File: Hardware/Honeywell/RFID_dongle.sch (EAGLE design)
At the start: 11 parts, among them J1 USB_B_PTH, J2 USB_A_PTH_MALE, J5 1X2-3.5MM, J6 1X2-3.5MM, Q1 35A/25V/8.5mΩ

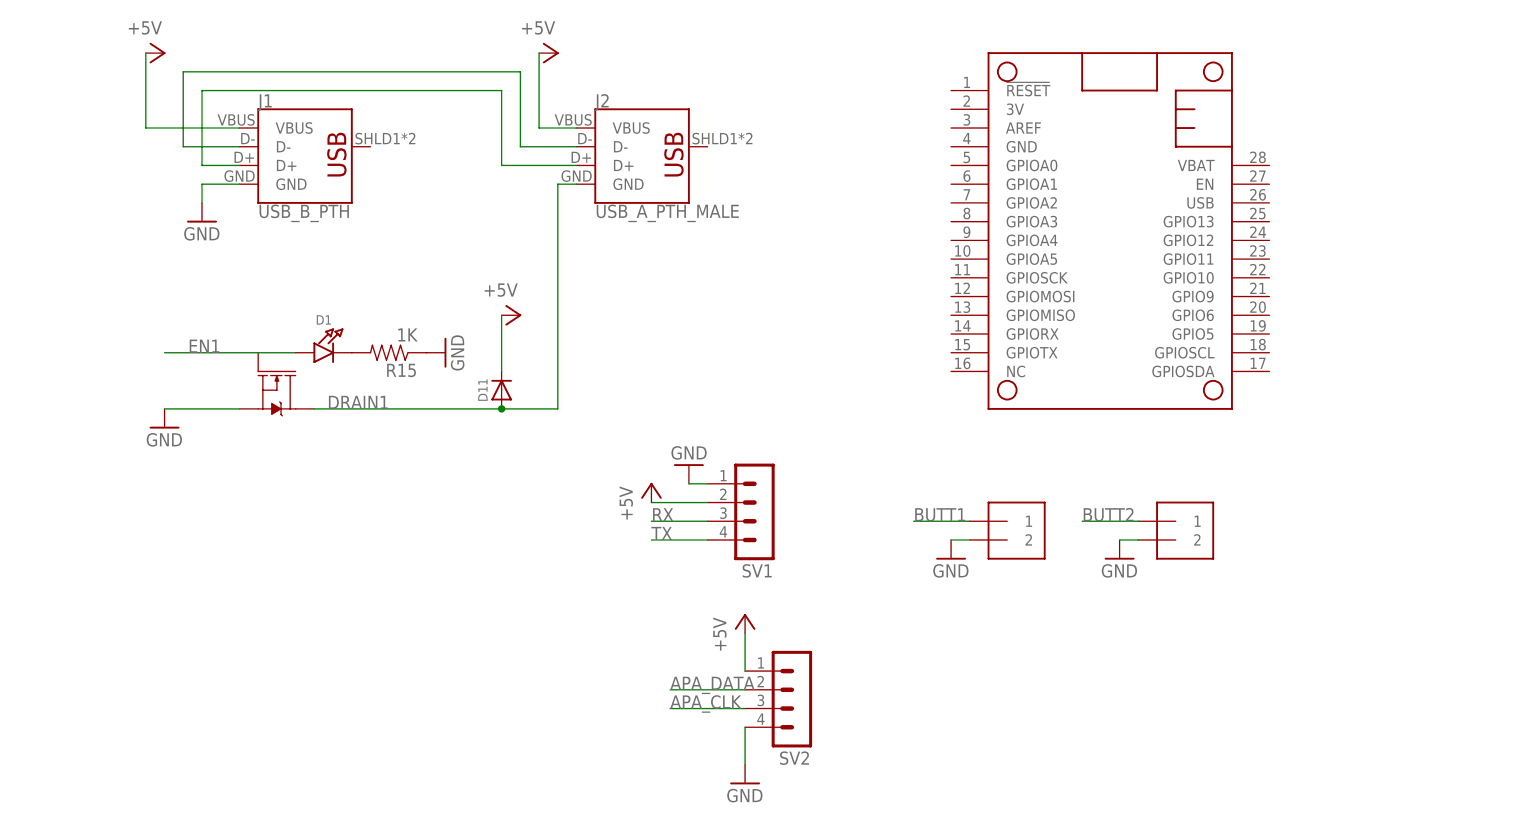
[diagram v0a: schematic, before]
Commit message: HEEP-878 WIP, to be converted to USB switch IC
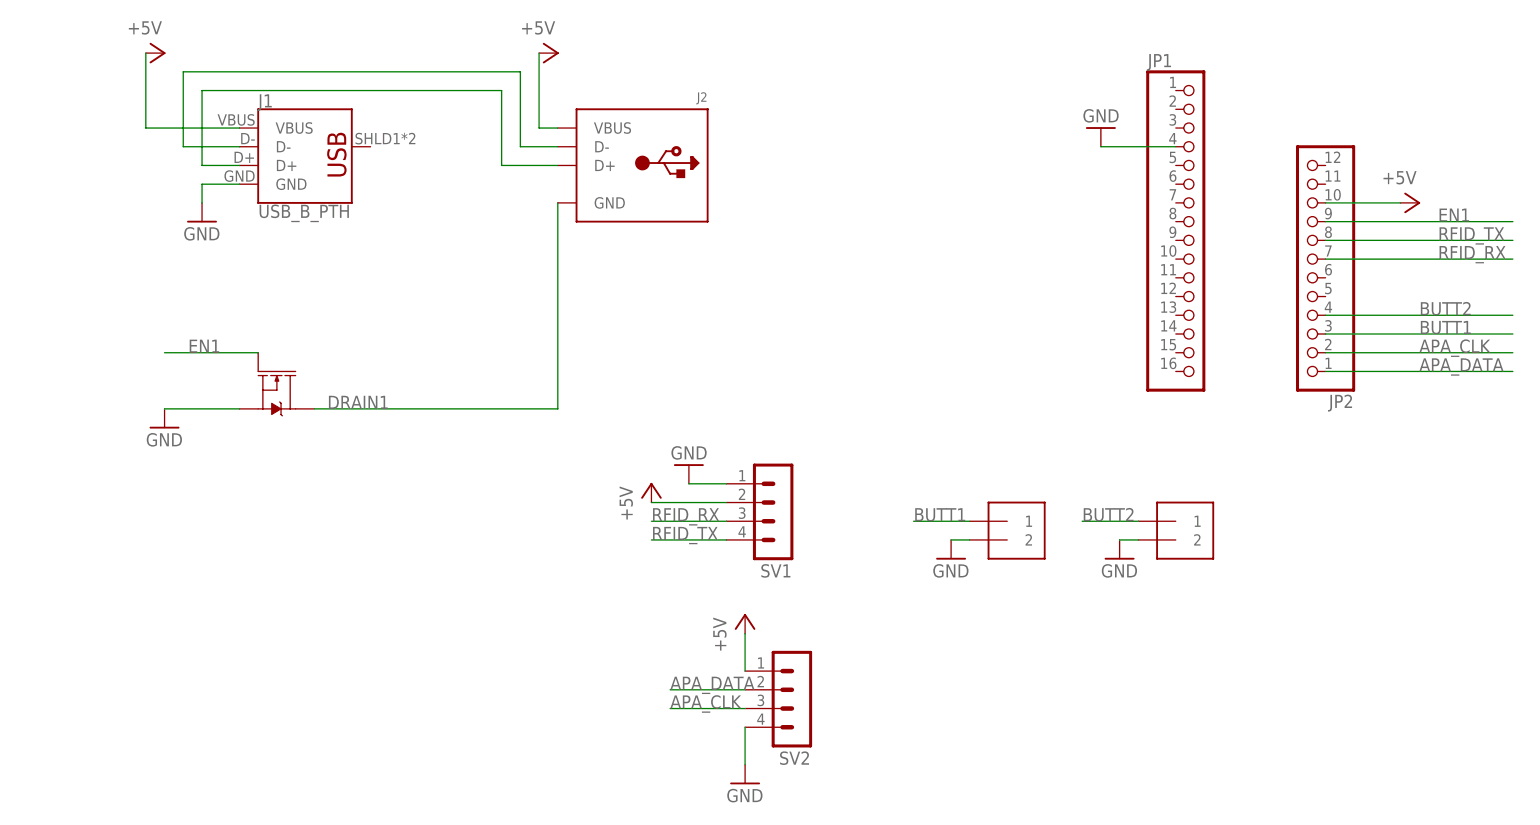
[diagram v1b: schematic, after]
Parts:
- removed D1: (no value), microbuilder:LED0805_NOOUTLINE
- removed D11: (no value), microbuilder:DIODESOD-123
- removed MS1: FEATHERWING_NODIM, adafruit:FEATHERWING_NODIM
- removed R15: 1K, SparkFun-Passives:RESISTOR0805-RES
- added JP1: (no value), microbuilder:HEADER-1X16_MIN
- added JP2: (no value), microbuilder:HEADER-1X12_MIN
- J2: value USB_A_PTH_MALE -> (none); device SparkFun-Connectors:USB_A_PTH_MALE -> microbuilder:USB_TYPEAPTHFML
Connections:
- removed net N$5: D1.C, R15.2
- removed net RX: SV1.3
- removed net TX: SV1.4
- new net RFID_RX: JP2.7, SV1.3
- new net RFID_TX: JP2.8, SV1.4
- net +5V: now also JP2.10; no longer D11.C
- net APA_CLK: now also JP2.2
- net APA_DATA: now also JP2.1
- net BUTT1: now also JP2.3
- net BUTT2: now also JP2.4
- net DRAIN1: no longer D11.A
- net EN1: now also JP2.9; no longer D1.A
- net GND: now also JP1.4; no longer R15.1
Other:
- moved on the sheet: SV1

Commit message: HEEP-878 working USB switch design, added USB switch IC to library
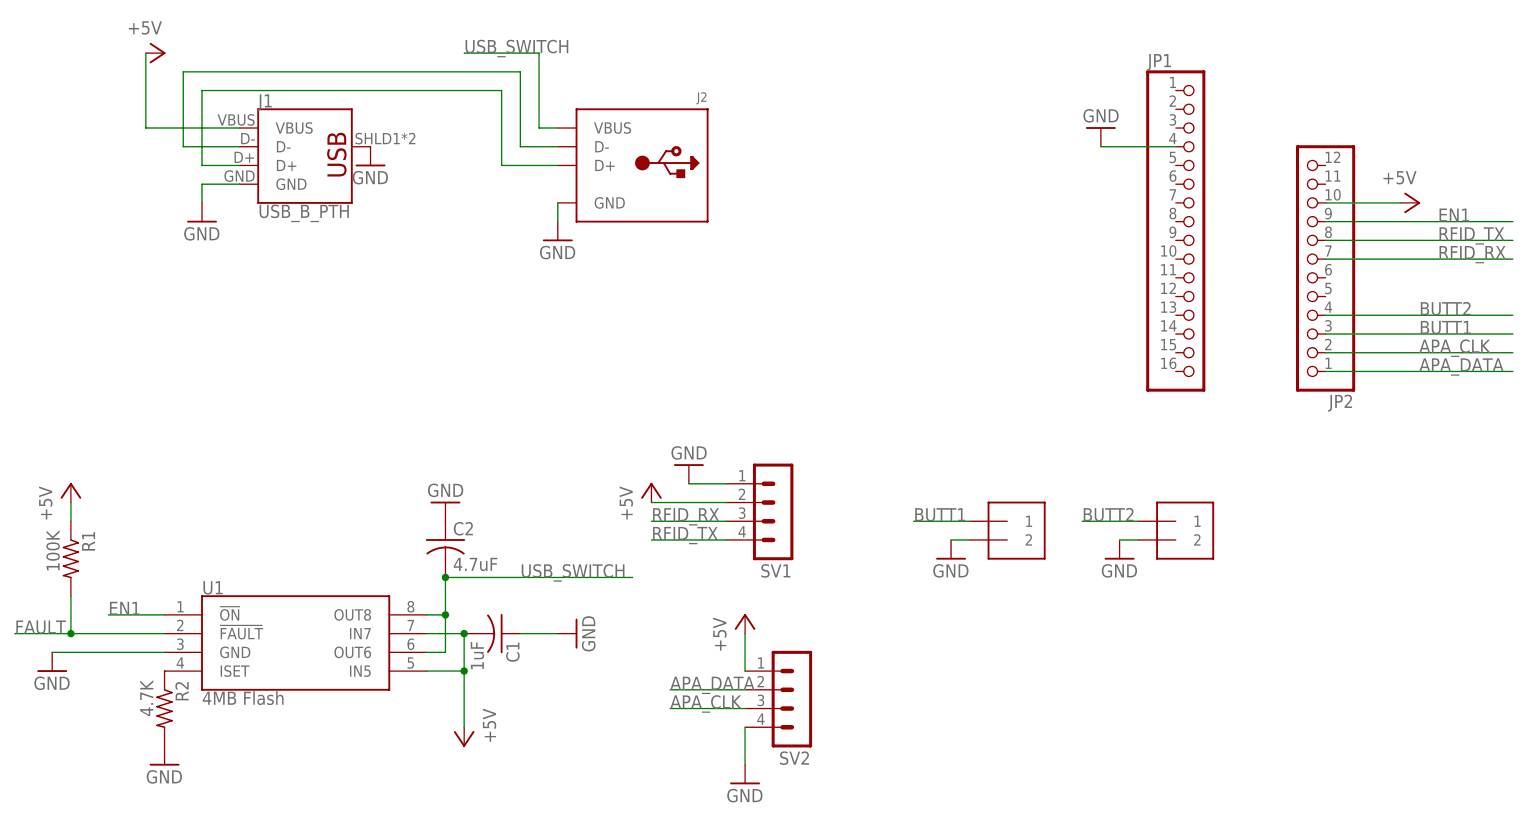
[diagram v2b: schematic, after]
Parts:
- removed Q1: 35A/25V/8.5mΩ, SparkFun-DiscreteSemi:MOSFET-NCH-FDD8780
- added C1: 1uF, adafruit:C-USC0805K
- added C2: 4.7uF, adafruit:C-USC0805K
- added R1: 100K, adafruit:R-US_R0805
- added R2: 4.7K, adafruit:R-US_R0805
- added U1: 4MB Flash, Heep:AT25SF041
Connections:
- removed net DRAIN1: J2.GND, Q1.D
- new net FAULT: R1.2, U1.!FAULT
- new net N$1: R2.1, U1.ISET
- new net USB_SWITCH: C2.2, J2.VBUS, U1.OUT6, U1.OUT8
- net +5V: now also C1.2, R1.1, U1.IN5, U1.IN7; no longer J2.VBUS
- net EN1: now also U1.!ON; no longer Q1.G
- net GND: now also C1.1, C2.1, J1.SHIELD, J2.GND, R2.2, U1.GND; no longer Q1.S
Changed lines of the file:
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@@
 <part name="J2" library="microbuilder" deviceset="USB_TYPEA" device="PTHFML"/>
 <part name="GND1" library="supply1" library_urn="urn:adsk.eagle:library:371" deviceset="GND" device=""/>
-<part name="GND5" library="SparkFun-Aesthetics" deviceset="GND" device=""/>
-<part name="Q1" library="SparkFun-DiscreteSemi" deviceset="MOSFET-NCH" device="-FDD8780" value="35A/25V/8.5mΩ"/>
-<part name="P+1" library="supply1" library_urn="urn:adsk.eagle:library:371" deviceset="+5V" device=""/>
 <part name="P+2" library="supply1" library_urn="urn:adsk.eagle:library:371" deviceset="+5V" device=""/>
 <part name="P+4" library="supply1" library_urn="urn:adsk.eagle:library:371" deviceset="+5V" device=""/>
@@
 <part name="GND8" library="SparkFun-Aesthetics" deviceset="GND" device=""/>
 <part name="P+6" library="supply1" library_urn="urn:adsk.eagle:library:371" deviceset="+5V" device=""/>
+<part name="U1" library="Heep" deviceset="AT25SF041" device="" value="4MB Flash"/>
+<part name="GND4" library="SparkFun-Aesthetics" deviceset="GND" device=""/>
+<part name="P+3" library="supply1" library_urn="urn:adsk.eagle:library:371" deviceset="+5V" device=""/>
+<part name="GND9" library="supply1" library_urn="urn:adsk.eagle:library:371" deviceset="GND" device=""/>
+<part name="C1" library="adafruit" library_urn="urn:adsk.eagle:library:420" deviceset="C-US" device="C0805K" value="1uF"/>
+<part name="GND5" library="SparkFun-Aesthetics" deviceset="GND" device=""/>
+<part name="C2" library="adafruit" library_urn="urn:adsk.eagle:library:420" deviceset="C-US" device="C0805K" value="4.7uF"/>
+<part name="GND10" library="SparkFun-Aesthetics" deviceset="GND" device=""/>
+<part name="R1" library="adafruit" library_urn="urn:adsk.eagle:library:420" deviceset="R-US_" device="R0805" value="100K"/>
+<part name="P+1" library="supply1" library_urn="urn:adsk.eagle:library:371" deviceset="+5V" device=""/>
+<part name="R2" library="adafruit" library_urn="urn:adsk.eagle:library:420" deviceset="R-US_" device="R0805" value="4.7K"/>
+<part name="GND11" library="SparkFun-Aesthetics" deviceset="GND" device=""/>
+<part name="GND12" library="supply1" library_urn="urn:adsk.eagle:library:371" deviceset="GND" device=""/>
 </parts>
 <sheets>
@@
 <instance part="J2" gate="G$1" x="63.5" y="40.64" rot="MR0"/>
 <instance part="GND1" gate="1" x="5.08" y="33.02"/>
-<instance part="GND5" gate="1" x="0" y="5.08"/>
-<instance part="Q1" gate="NMOS" x="15.24" y="10.16" smashed="yes" rot="R270"/>
-<instance part="P+1" gate="1" x="53.34" y="55.88" rot="R270"/>
 <instance part="P+2" gate="1" x="0" y="55.88" rot="R270"/>
 <instance part="P+4" gate="1" x="66.04" y="-2.54"/>
@@
 <instance part="GND8" gate="1" x="127" y="45.72" rot="R180"/>
 <instance part="P+6" gate="1" x="170.18" y="35.56" rot="R270"/>
+<instance part="U1" gate="G$1" x="15.24" y="-25.4"/>
+<instance part="GND4" gate="1" x="-15.24" y="-27.94"/>
+<instance part="P+3" gate="1" x="40.64" y="-38.1" rot="R180"/>
+<instance part="GND9" gate="1" x="53.34" y="30.48"/>
+<instance part="C1" gate="G$1" x="45.72" y="-22.86" rot="R270"/>
+<instance part="GND5" gate="1" x="55.88" y="-22.86" rot="R90"/>
+<instance part="C2" gate="G$1" x="38.1" y="-10.16"/>
+<instance part="GND10" gate="1" x="38.1" y="-5.08" rot="R180"/>
+<instance part="R1" gate="G$1" x="-12.7" y="-12.7" rot="R270"/>
+<instance part="P+1" gate="1" x="-12.7" y="-2.54"/>
+<instance part="R2" gate="G$1" x="0" y="-33.02" rot="R270"/>
+<instance part="GND11" gate="1" x="0" y="-40.64"/>
+<instance part="GND12" gate="1" x="27.94" y="40.64"/>
 </instances>
 <busses>
@@
 </segment>
 <segment>
-<pinref part="GND5" gate="1" pin="GND"/>
-<pinref part="Q1" gate="NMOS" pin="S"/>
-<wire x1="0" y1="7.62" x2="10.16" y2="7.62" width="0.1524" layer="91"/>
-</segment>
-<segment>
 <pinref part="GND2" gate="1" pin="GND"/>
 <wire x1="71.12" y1="-2.54" x2="76.2" y2="-2.54" width="0.1524" layer="91"/>
@@
 <wire x1="127" y1="43.18" x2="137.16" y2="43.18" width="0.1524" layer="91"/>
 </segment>
+<segment>
+<pinref part="U1" gate="G$1" pin="GND"/>
+<pinref part="GND4" gate="1" pin="GND"/>
+<wire x1="-15.24" y1="-25.4" x2="0" y2="-25.4" width="0.1524" layer="91"/>
+</segment>
+<segment>
+<pinref part="J2" gate="G$1" pin="GND"/>
+<pinref part="GND9" gate="1" pin="GND"/>
+<wire x1="53.34" y1="33.02" x2="53.34" y2="35.56" width="0.1524" layer="91"/>
+</segment>
+<segment>
+<pinref part="C1" gate="G$1" pin="1"/>
+<pinref part="GND5" gate="1" pin="GND"/>
+<wire x1="53.34" y1="-22.86" x2="48.26" y2="-22.86" width="0.1524" layer="91"/>
+</segment>
+<segment>
+<pinref part="C2" gate="G$1" pin="1"/>
+<pinref part="GND10" gate="1" pin="GND"/>
+</segment>
+<segment>
+<pinref part="R2" gate="G$1" pin="2"/>
+<pinref part="GND11" gate="1" pin="GND"/>
+</segment>
+<segment>
+<pinref part="J1" gate="G$1" pin="SHIELD"/>
+<pinref part="GND12" gate="1" pin="GND"/>
+</segment>
 </net>
 <net name="EN1" class="0">
-<segment>
-<label x="7.62" y="15.24" size="1.778" layer="95" rot="MR0"/>
-<pinref part="Q1" gate="NMOS" pin="G"/>
-<wire x1="0" y1="15.24" x2="12.7" y2="15.24" width="0.1524" layer="91"/>
-</segment>
 <segment>
 <pinref part="JP2" gate="G$1" pin="9"/>
@@
 <label x="172.72" y="33.02" size="1.778" layer="95"/>
 </segment>
-</net>
-<net name="DRAIN1" class="0">
-<segment>
-<label x="30.48" y="7.62" size="1.778" layer="95" rot="MR0"/>
-<pinref part="Q1" gate="NMOS" pin="D"/>
-<wire x1="53.34" y1="7.62" x2="20.32" y2="7.62" width="0.1524" layer="91"/>
-<pinref part="J2" gate="G$1" pin="GND"/>
-<wire x1="53.34" y1="35.56" x2="53.34" y2="7.62" width="0.1524" layer="91"/>
+<segment>
+<wire x1="-7.62" y1="-20.32" x2="0" y2="-20.32" width="0.1524" layer="91"/>
+<pinref part="U1" gate="G$1" pin="!ON"/>
+<label x="-7.62" y="-20.32" size="1.778" layer="95"/>
 </segment>
 </net>
 <net name="+5V" class="0">
-<segment>
-<pinref part="P+1" gate="1" pin="+5V"/>
-<pinref part="J2" gate="G$1" pin="VBUS"/>
-<wire x1="53.34" y1="45.72" x2="50.8" y2="45.72" width="0.1524" layer="91"/>
-<wire x1="50.8" y1="45.72" x2="50.8" y2="55.88" width="0.1524" layer="91"/>
-</segment>
 <segment>
 <pinref part="J1" gate="G$1" pin="VBUS"/>
@@
 <wire x1="167.64" y1="35.56" x2="157.48" y2="35.56" width="0.1524" layer="91"/>
 </segment>
+<segment>
+<pinref part="U1" gate="G$1" pin="IN7"/>
+<wire x1="35.56" y1="-22.86" x2="40.64" y2="-22.86" width="0.1524" layer="91"/>
+<wire x1="40.64" y1="-22.86" x2="40.64" y2="-27.94" width="0.1524" layer="91"/>
+<pinref part="U1" gate="G$1" pin="IN5"/>
+<wire x1="40.64" y1="-27.94" x2="40.64" y2="-35.56" width="0.1524" layer="91"/>
+<wire x1="35.56" y1="-27.94" x2="40.64" y2="-27.94" width="0.1524" layer="91"/>
+<junction x="40.64" y="-27.94"/>
+<pinref part="P+3" gate="1" pin="+5V"/>
+<pinref part="C1" gate="G$1" pin="2"/>
+<junction x="40.64" y="-22.86"/>
+</segment>
+<segment>
+<pinref part="R1" gate="G$1" pin="1"/>
+<pinref part="P+1" gate="1" pin="+5V"/>
+<wire x1="-12.7" y1="-5.08" x2="-12.7" y2="-7.62" width="0.1524" layer="91"/>
+</segment>
 </net>
 <net name="BUTT1" class="0">
@@
 </segment>
 </net>
+<net name="USB_SWITCH" class="0">
+<segment>
+<pinref part="J2" gate="G$1" pin="VBUS"/>
+<wire x1="53.34" y1="45.72" x2="50.8" y2="45.72" width="0.1524" layer="91"/>
+<wire x1="50.8" y1="45.72" x2="50.8" y2="55.88" width="0.1524" layer="91"/>
+<wire x1="50.8" y1="55.88" x2="40.64" y2="55.88" width="0.1524" layer="91"/>
+<label x="40.64" y="55.88" size="1.778" layer="95"/>
+</segment>
+<segment>
+<pinref part="U1" gate="G$1" pin="OUT6"/>
+<wire x1="35.56" y1="-25.4" x2="38.1" y2="-25.4" width="0.1524" layer="91"/>
+<wire x1="38.1" y1="-25.4" x2="38.1" y2="-20.32" width="0.1524" layer="91"/>
+<pinref part="U1" gate="G$1" pin="OUT8"/>
+<wire x1="38.1" y1="-20.32" x2="38.1" y2="-15.24" width="0.1524" layer="91"/>
+<wire x1="35.56" y1="-20.32" x2="38.1" y2="-20.32" width="0.1524" layer="91"/>
+<junction x="38.1" y="-20.32"/>
+<wire x1="38.1" y1="-15.24" x2="63.5" y2="-15.24" width="0.1524" layer="91"/>
+<label x="48.26" y="-15.24" size="1.778" layer="95"/>
+<pinref part="C2" gate="G$1" pin="2"/>
+<junction x="38.1" y="-15.24"/>
+</segment>
+</net>
+<net name="FAULT" class="0">
+<segment>
+<pinref part="U1" gate="G$1" pin="!FAULT"/>
+<wire x1="-20.32" y1="-22.86" x2="-12.7" y2="-22.86" width="0.1524" layer="91"/>
+<label x="-20.32" y="-22.86" size="1.778" layer="95"/>
+<pinref part="R1" gate="G$1" pin="2"/>
+<wire x1="-12.7" y1="-22.86" x2="0" y2="-22.86" width="0.1524" layer="91"/>
+<wire x1="-12.7" y1="-17.78" x2="-12.7" y2="-22.86" width="0.1524" layer="91"/>
+<junction x="-12.7" y="-22.86"/>
+</segment>
+</net>
+<net name="N$1" class="0">
+<segment>
+<pinref part="U1" gate="G$1" pin="ISET"/>
+<pinref part="R2" gate="G$1" pin="1"/>
+</segment>
+</net>
